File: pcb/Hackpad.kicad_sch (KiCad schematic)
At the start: 15 parts, among them J1 OLED_DISPLAY, SW1 SW_Push, SW2 SW_Push, SW3 SW_Push, SW4 SW_Push, SW5 SW_Push, SW6 SW_Push, SW7 RotaryEncoder_Switch, U1 MOUDLE-SEEEDUINO-XIAO

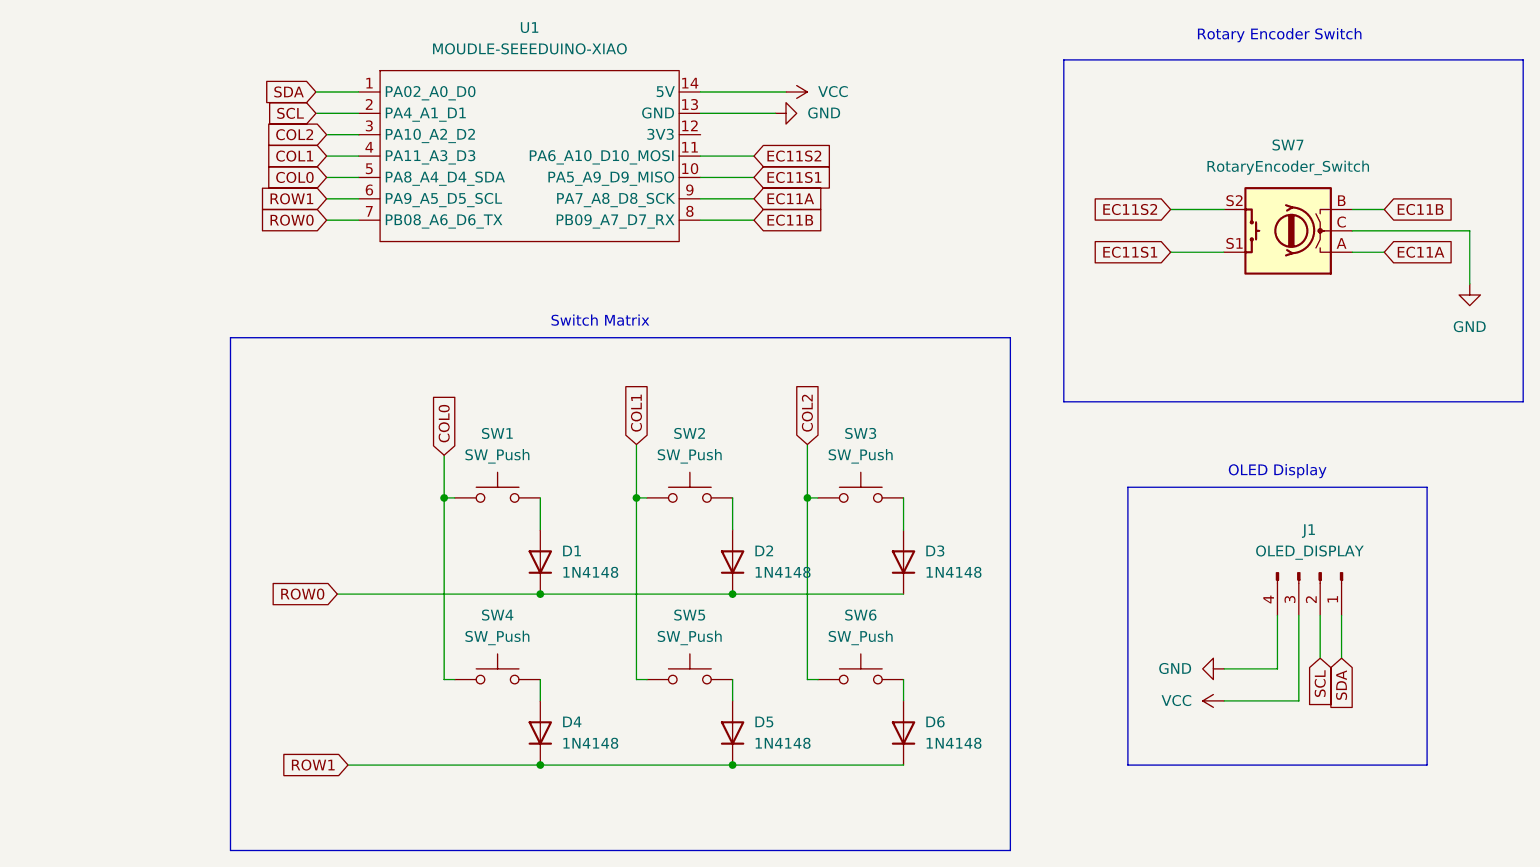
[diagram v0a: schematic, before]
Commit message: Fixes + Adding new files
- Added new cats on the PCB
- Adjusted the PCB and routed everything again
- Adjusted the schematic
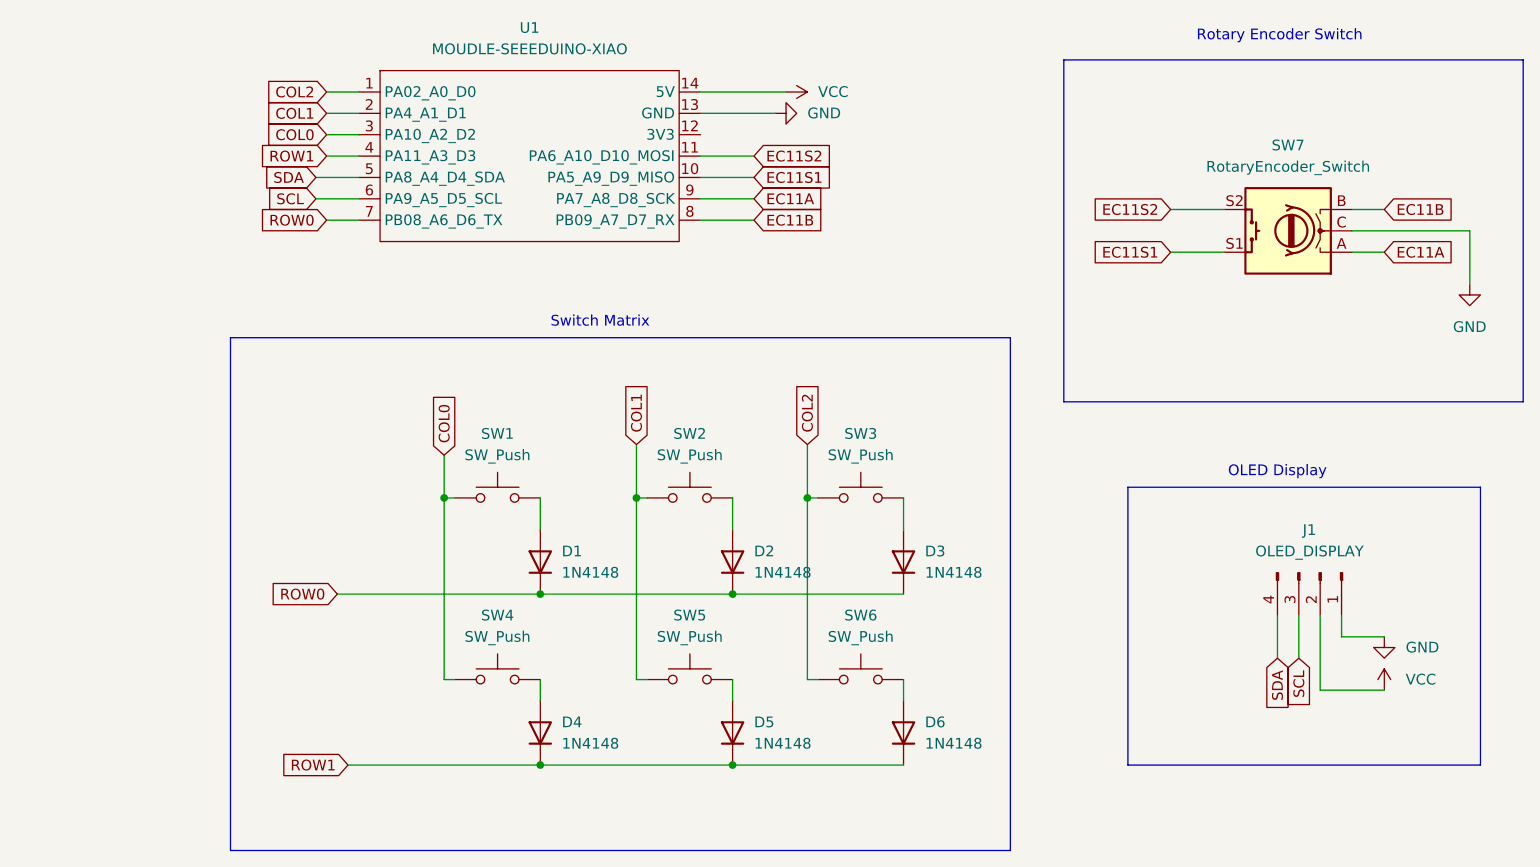
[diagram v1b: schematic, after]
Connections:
- net COL0: now also U1.3 (PA10_A2_D2); no longer U1.5 (PA8_A4_D4_SDA)
- net COL1: now also U1.2 (PA4_A1_D1); no longer U1.4 (PA11_A3_D3)
- net COL2: now also U1.1 (PA02_A0_D0); no longer U1.3 (PA10_A2_D2)
- net GND: now also J1.1 (Pin_1); no longer J1.4 (Pin_4)
- net ROW1: now also U1.4 (PA11_A3_D3); no longer U1.6 (PA9_A5_D5_SCL)
- net SCL: now also J1.3 (Pin_3), U1.6 (PA9_A5_D5_SCL); no longer J1.2 (Pin_2), U1.2 (PA4_A1_D1)
- net SDA: now also J1.4 (Pin_4), U1.5 (PA8_A4_D4_SDA); no longer J1.1 (Pin_1), U1.1 (PA02_A0_D0)
- net VCC: now also J1.2 (Pin_2); no longer J1.3 (Pin_3)

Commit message: Fixes and new files added
- Added .step files of the case
- Added .step file of the whole macropad
- Added the firmware
- Modified the readme.md
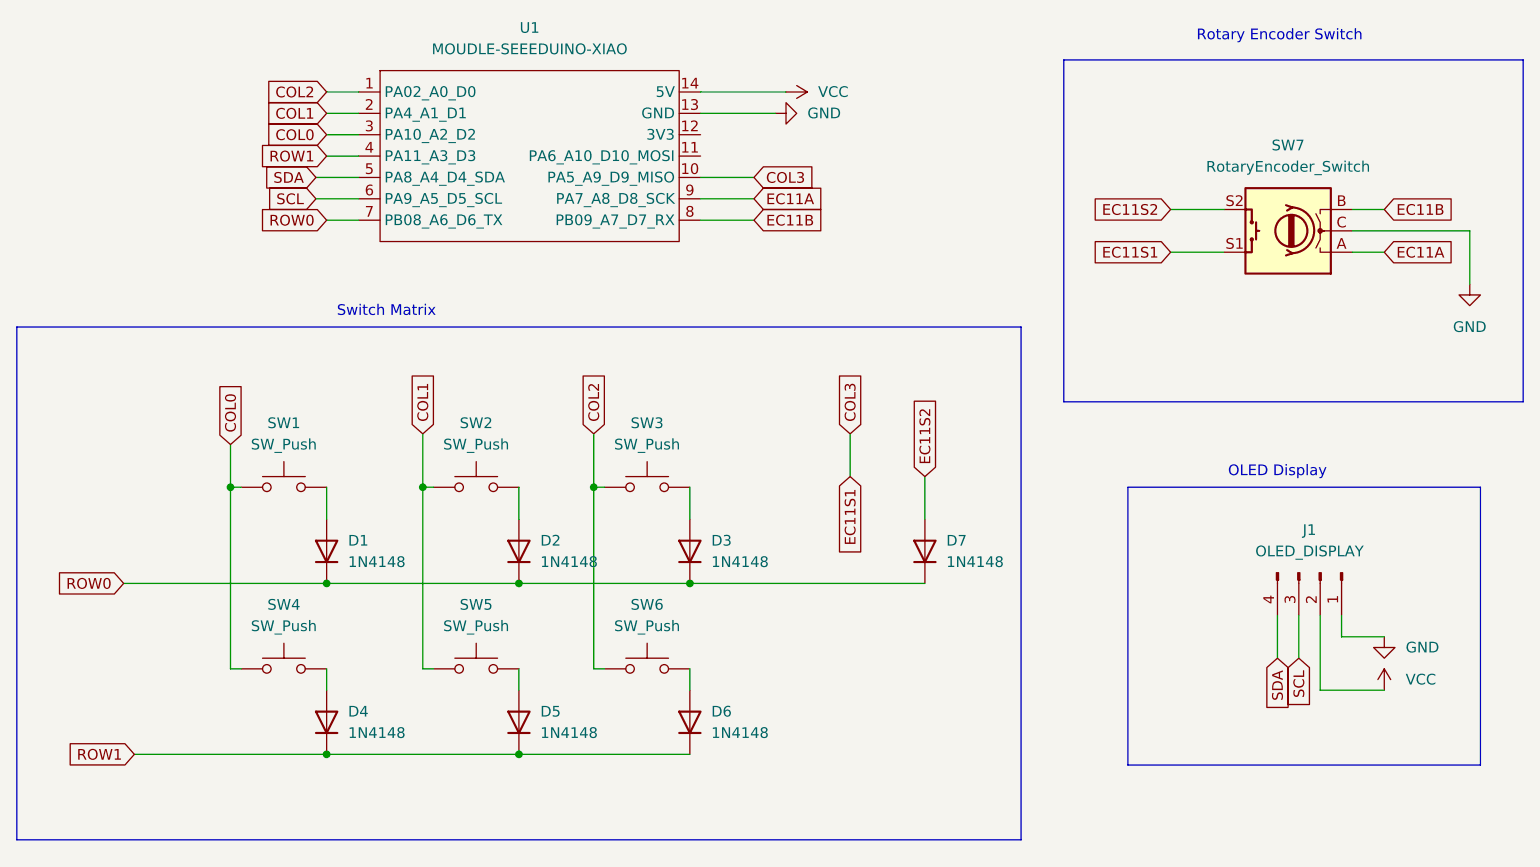
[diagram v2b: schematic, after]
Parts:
- added D7: 1N4148, Diode_THT:D_DO-35_SOD27_P7.62mm_Horizontal, symbol Diode:1N4148
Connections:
- net EC11S2: now also D7.2 (A); no longer U1.11 (PA6_A10_D10_MOSI)
- net ROW0: now also D7.1 (K)
- net EC11S1 renamed COL3
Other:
- moved on the sheet: D1, D2, D3, D4, D5, D6, SW1, SW2, SW3, SW4, SW5, SW6
